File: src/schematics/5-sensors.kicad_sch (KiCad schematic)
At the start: 13 parts, among them Q501 NX6008NBKW, Q502 NX6008NBKW, U501 TPS7A2028PDBVR, U502 DPS310XTSA1

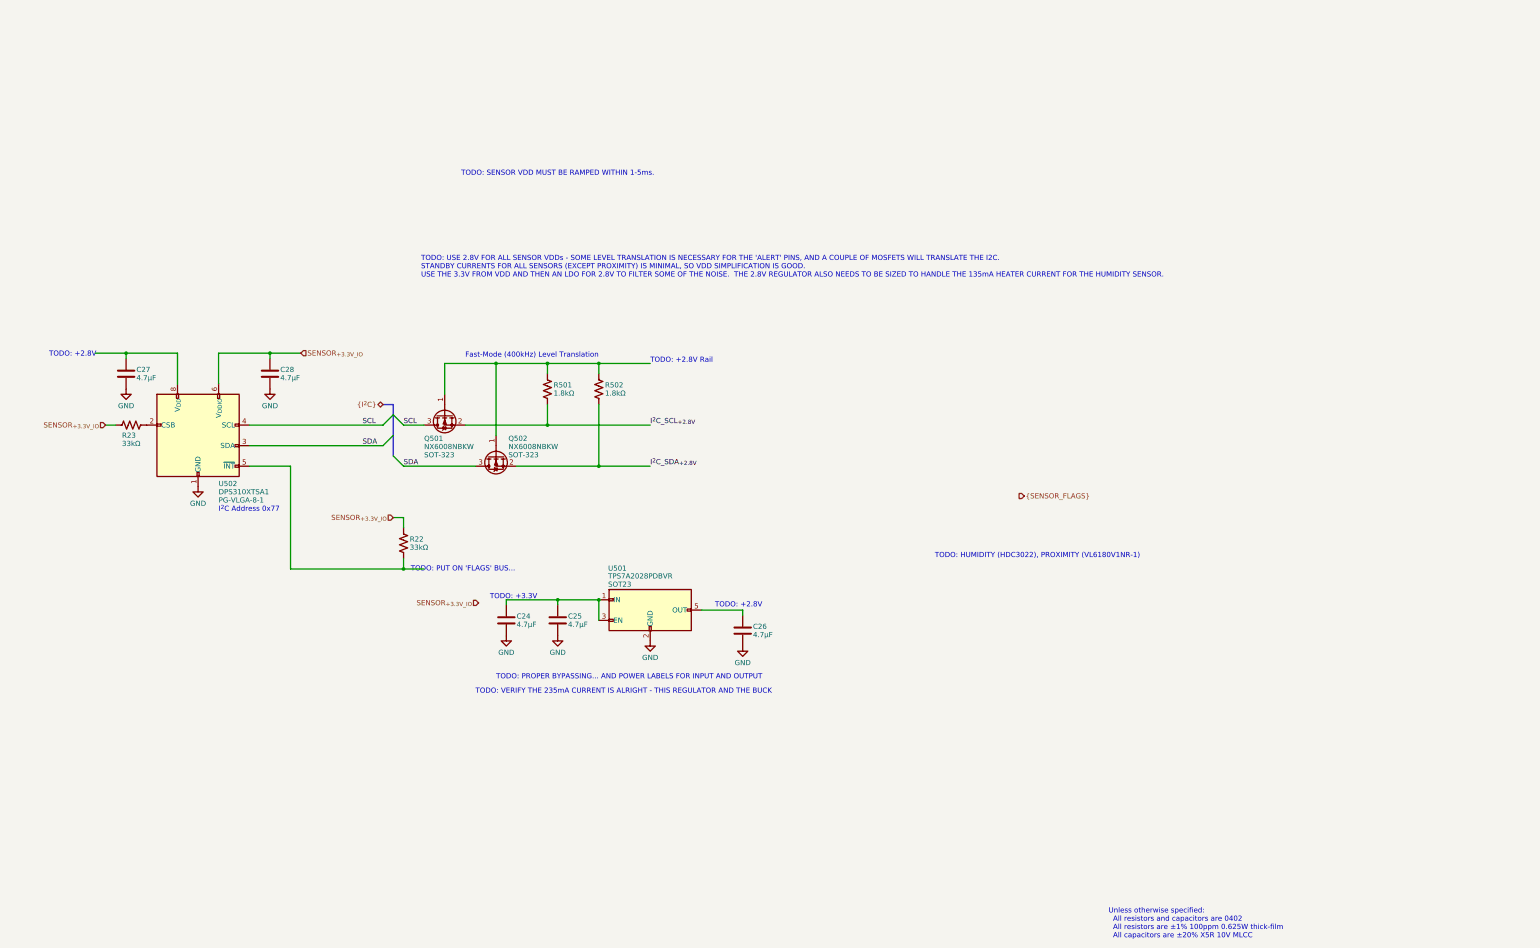
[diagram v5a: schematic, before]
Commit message: Drew the schematic for the sensors.
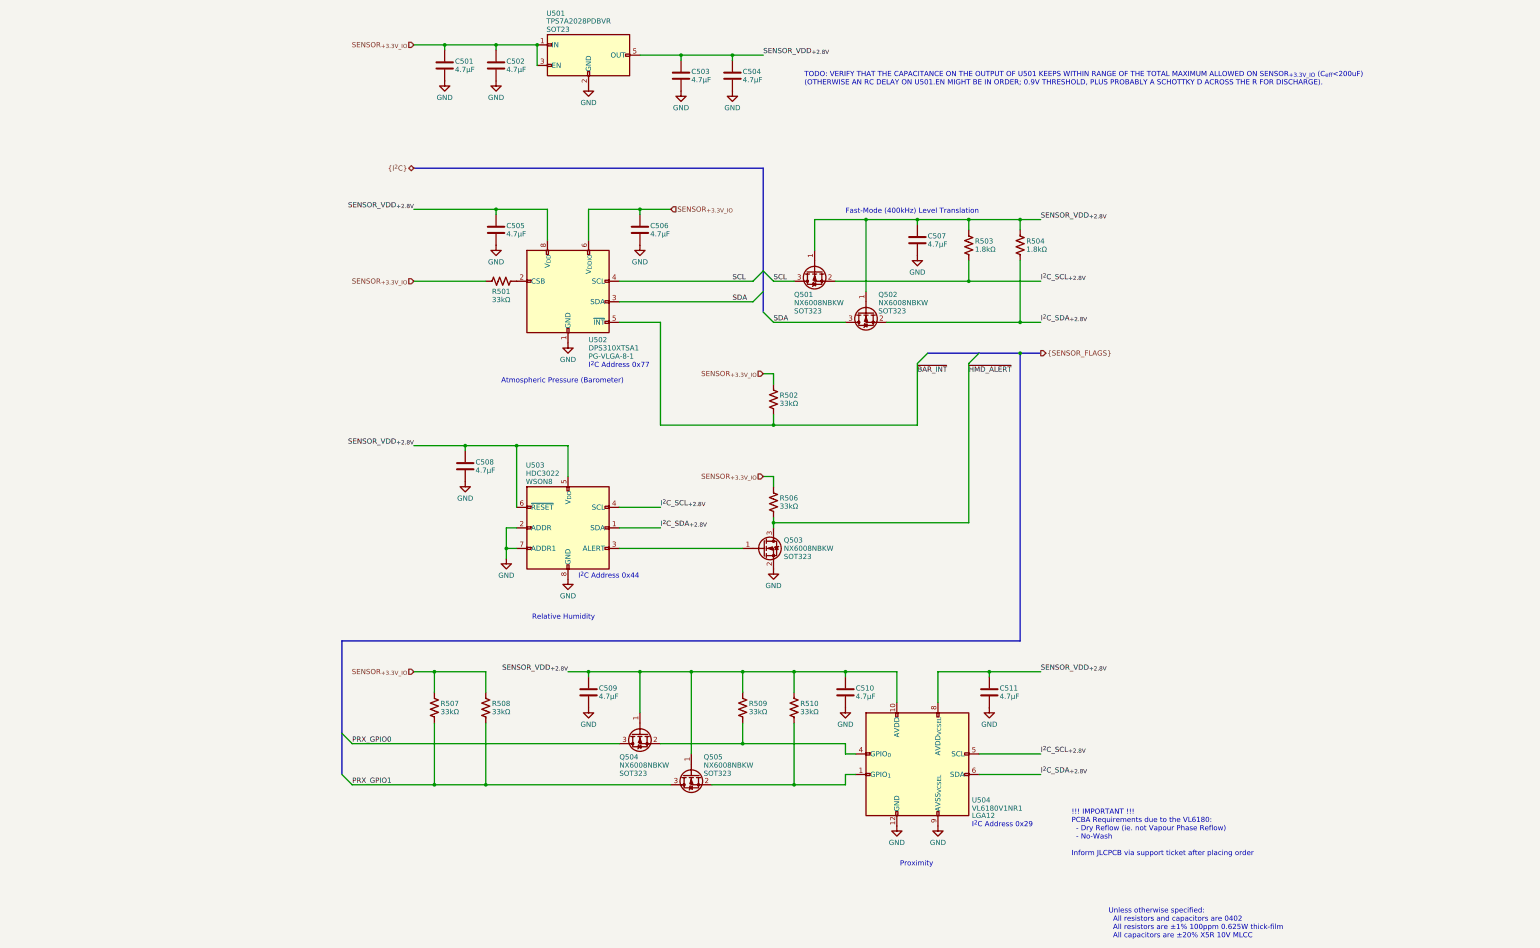
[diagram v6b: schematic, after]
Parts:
- added C504, C507, C508, C509, C510, C511: 4.7μF, restall-generic-capacitors:unpolarised-nominal-0402-1005, symbol restall-generic-capacitors:capacitor-unpolarised
- added Q503, Q504, Q505: NX6008NBKW, restall-generic-sot:SOT323, symbol restall-manufacturer-nexperia:NX6008NBKW
- added R506, R507, R508, R509, R510: 33kΩ, restall-generic-resistors:nominal-0402-1005, symbol restall-generic-resistors:resistor
- added U503: HDC3022, restall-manufacturer-ti:WSON8-2.5x2.5mm-0.5mm-expad-1.2x1.9mm-thermvias, symbol restall-manufacturer-ti:HDC302?
- added U504: VL6180V1NR1, restall-manufacturer-st:OPTICAL-LGA12-2.8x4.8mm-0.75mm, symbol restall-manufacturer-st:VL6180V1NR1
- Q501, Q502: footprint restall-generic-sot:SOT-323 -> restall-generic-sot:SOT323; Package SOT-323 -> SOT323
- renumbered C24 to C501, C25 to C502, C26 to C503, C27 to C505, C28 to C506, R23 to R501, R22 to R502, R501 to R503, R502 to R504
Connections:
- net GND: now also C504.2, C507.2, C508.2, C509.2, C510.2, C511.2, Q503.2 (S), U503.2 (ADDR), U503.7 (ADDR1), U503.8 (GND), U503.9 (GND), U504.12 (GND), U504.9 (AVSS_{VCSEL})
- net I^{2}C_SCL_{+2.8V}: now also U503.4 (SCL), U504.5 (SCL)
- net I^{2}C_SDA_{+2.8V}: now also U503.1 (SDA), U504.6 (SDA)
- net SENSOR_{+3.3V_IO}: now also C501.1, C502.1, U501.1 (IN), U501.3 (EN), R506.1, R507.1, R508.1
- net SENSOR_VDD_{+2.8V}: now reaches C503.1, U501.5 (OUT)
- net SENSOR_VDD_{+2.8V}: now also C505.1, Q501.1 (G), Q502.1 (G), R503.1, R504.1, U502.8 (V_{DD}), C504.1, C507.1, C508.1, C509.1, C510.1, C511.1, Q504.1 (G), Q505.1 (G), R509.1, R510.1, U503.5 (V_{DD}), U503.6 (~{RESET}), U504.10 (AVDD), U504.8 (AVDD_{VCSEL})
- net ~{BAR_INT}: now reaches R502.2, U502.5 (SDO)
- new net: Q503.1 (G), U503.3 (ALERT)
- new net: Q505.2 (S), R510.2, U504.1 (GPIO_{1})
- new net: U504.11 (NC), U504.2 (NC), U504.3 (NC), U504.7 (NC)
- new net: Q504.2 (S), R509.2, U504.4 (GPIO_{0})
- new net PRX_GPIO0: Q504.3 (D)
- new net PRX_GPIO1: Q505.3 (D), R507.2, R508.2
- new net ~{HMD_ALERT}: Q503.3 (D), R506.2
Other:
- note added: "!!! IMPORTANT !!! PCBA Requirements due to the VL6180: - Dry Reflow (ie. not Vapour Phase Reflow) - No-Wash Inform JLCPCB via support ticket after placing order"
- note added: "Atmospheric Pressure (Barometer)"
- note added: "I^{2}C Address 0x29"
- note added: "I^{2}C Address 0x44"
- note added: "Proximity"
- note added: "Relative Humidity"
- note added: "TODO: VERIFY THAT THE CAPACITANCE ON THE OUTPUT OF U501 KEEPS WITHIN RANGE OF THE TOTAL MAXIMUM ALLOWED ON SENSOR_{+3.3V_IO} (C_{eff}<200uF) (OTHERWISE AN RC DELAY ON U501.EN MIGHT BE IN ORDER; 0.9V THRESHOLD, PLUS PROBABLY A SCHOTTKY D ACROSS THE R FOR DISCHARGE)."
- note removed: "TODO: +2.8V"
- note removed: "TODO: +2.8V Rail"
- note removed: "TODO: +3.3V"
- note removed: "TODO: HUMIDITY (HDC3022), PROXIMITY (VL6180V1NR-1)"
- note removed: "TODO: PROPER BYPASSING... AND POWER LABELS FOR INPUT AND OUTPUT"
- note removed: "TODO: PUT ON 'FLAGS' BUS..."
- note removed: "TODO: SENSOR VDD MUST BE RAMPED WITHIN 1-5ms."
- note removed: "TODO: USE 2.8V FOR ALL SENSOR VDDs - SOME LEVEL TRANSLATION IS NECESSARY FOR THE 'ALERT' PINS, AND A COUPLE OF MOSFETS WILL TRANSLATE THE I2C. STANDBY CURRENTS FOR ALL SENSORS (EXCEPT PROXIMITY) IS MINIMAL, SO VDD SIMPLIFICATION IS GOOD. USE THE 3.3V FROM VDD AND THEN AN LDO FOR 2.8V TO FILTER SOME OF THE NOISE. THE 2.8V REGULATOR ALSO NEEDS TO BE SIZED TO HANDLE THE 135mA HEATER CURRENT FOR THE 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"
- note removed: "TODO: VERIFY THE 235mA CURRENT IS ALRIGHT - THIS REGULATOR AND THE BUCK"
- moved on the sheet: C501, C502, C503, C505, C506, Q501, Q502, R501, R502, R503, R504, U501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

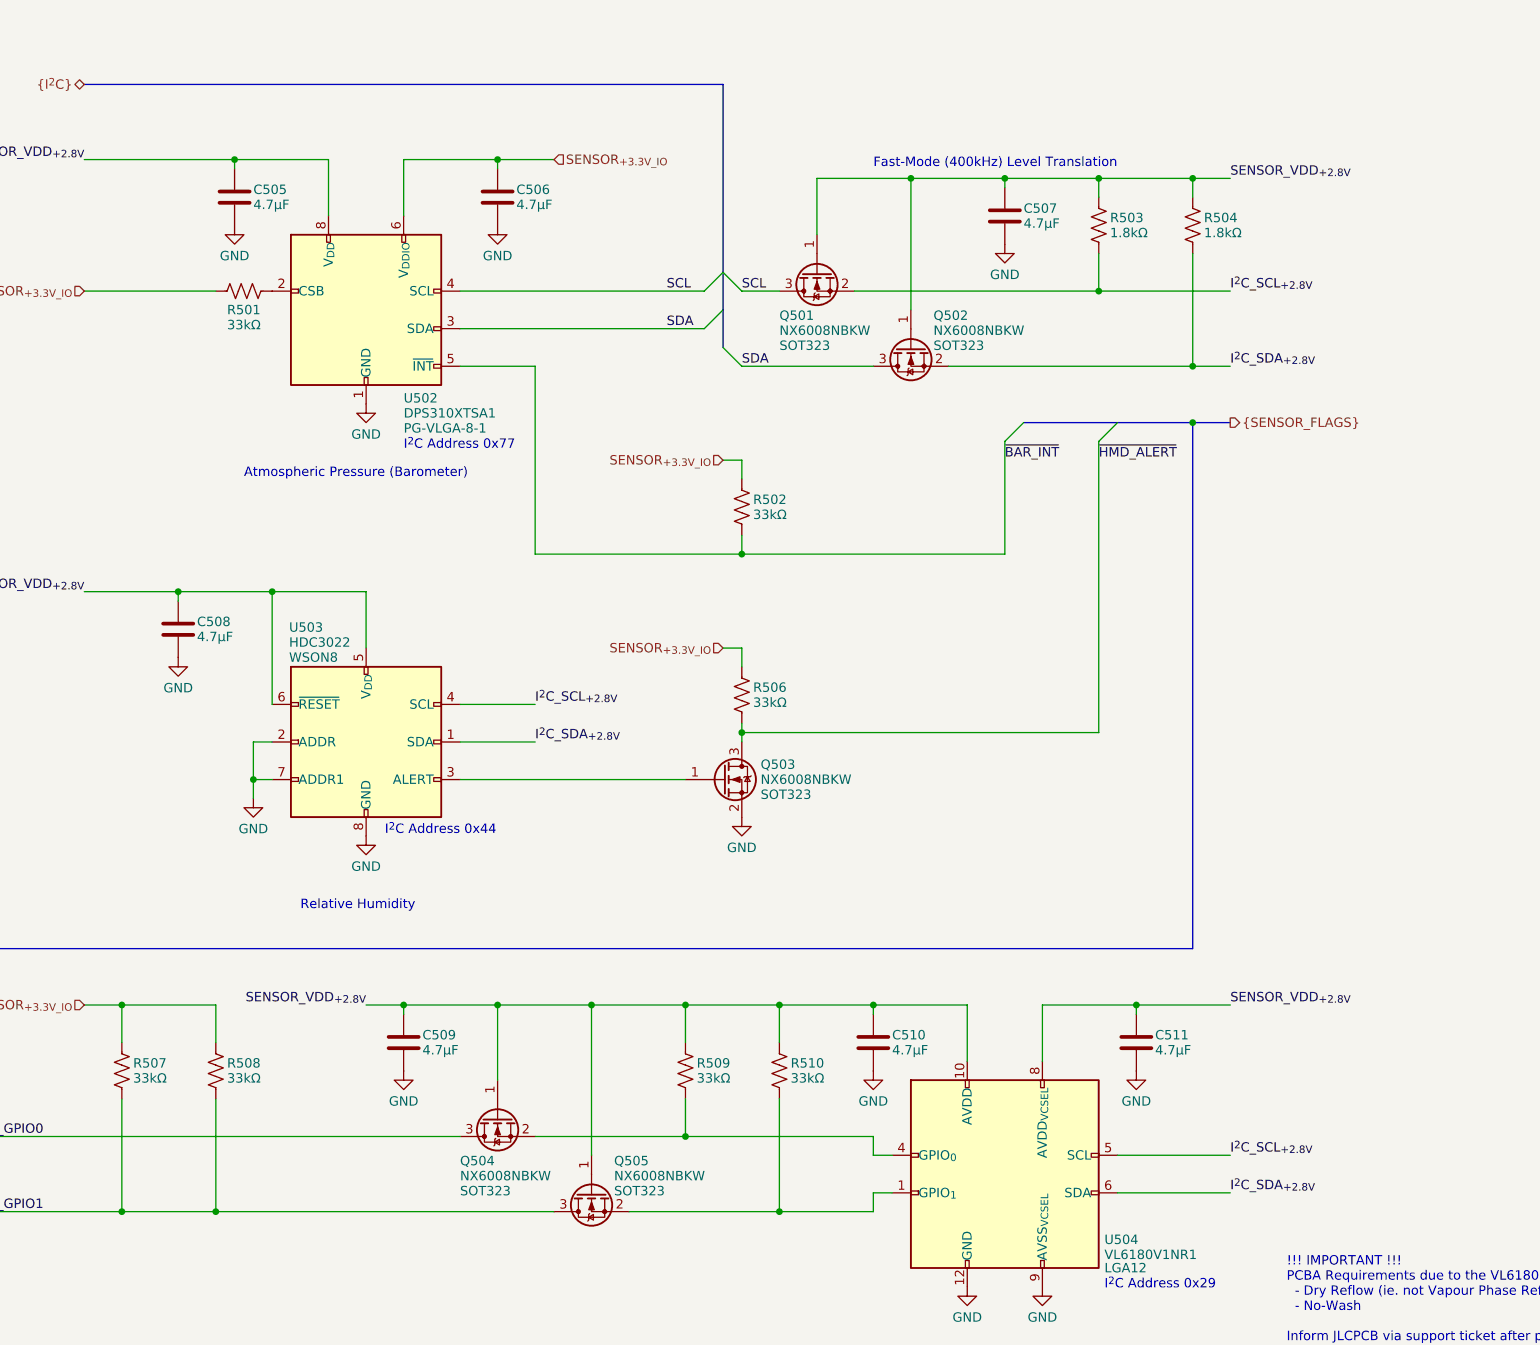
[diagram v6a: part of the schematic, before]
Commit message: Added gate resistors to reduce di/dt and thus supply noise.
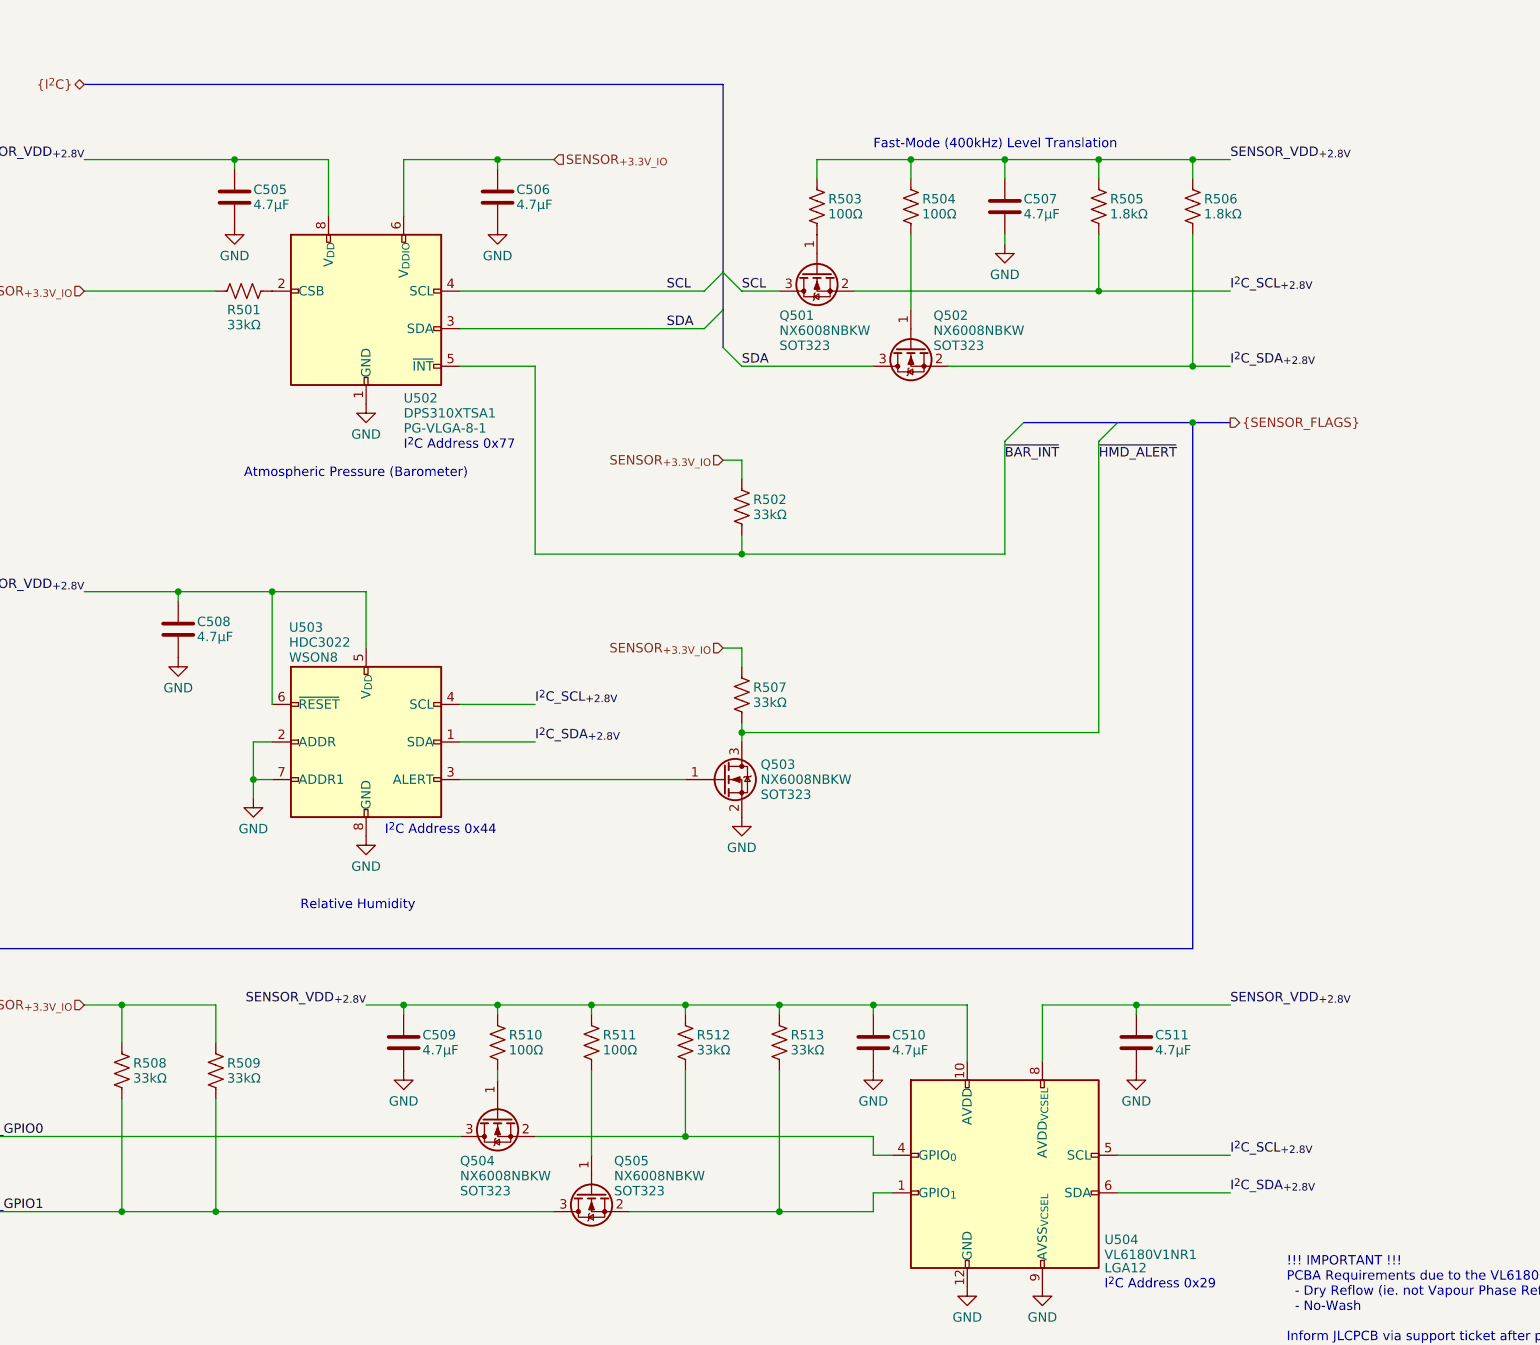
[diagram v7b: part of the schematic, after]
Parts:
- added R503, R504, R510, R511: 100Ω, restall-generic-resistors:nominal-0402-1005, symbol restall-generic-resistors:resistor
- renumbered R503 to R505, R504 to R506, R506 to R507, R507 to R508, R508 to R509, R509 to R512, R510 to R513
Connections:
- net SENSOR_VDD_{+2.8V}: now also R503.1, R504.1, R510.1, R511.1; no longer Q501.1 (G), Q502.1 (G), Q504.1 (G), Q505.1 (G)
- new net: Q501.1 (G), R503.2
- new net: Q502.1 (G), R504.2
- new net: Q504.1 (G), R510.2
- new net: Q505.1 (G), R511.2
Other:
- moved on the sheet: C507, R505, R506, R512, R513
